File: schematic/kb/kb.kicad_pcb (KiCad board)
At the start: 2 copper layers, 13.5 x 9.8 mm, 3 parts, among them P1 USB_A, SW1 Switch_SPDT_x2

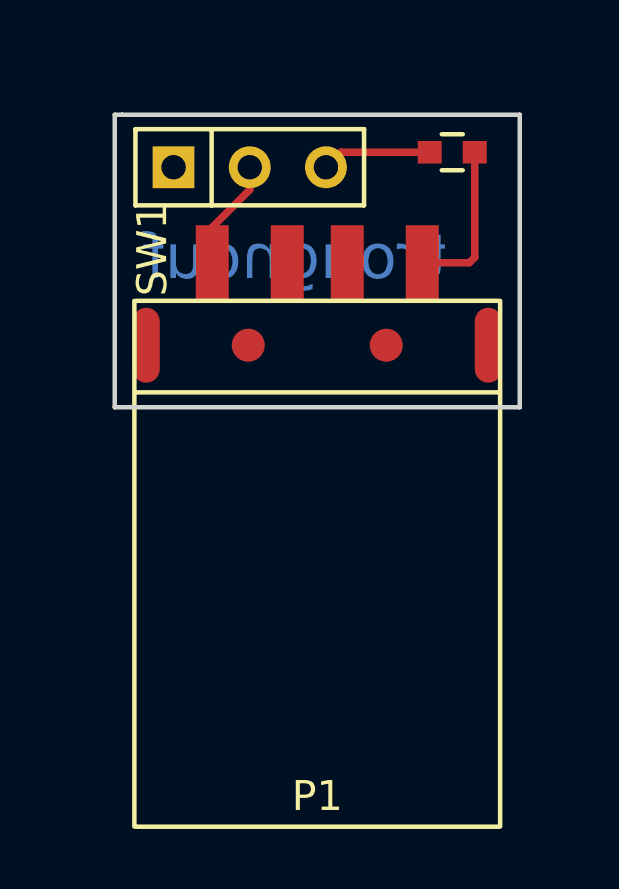
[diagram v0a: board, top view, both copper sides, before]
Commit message: Replaced single use fuse with resettable fuse (PPTC) on the keyboard-side adapter
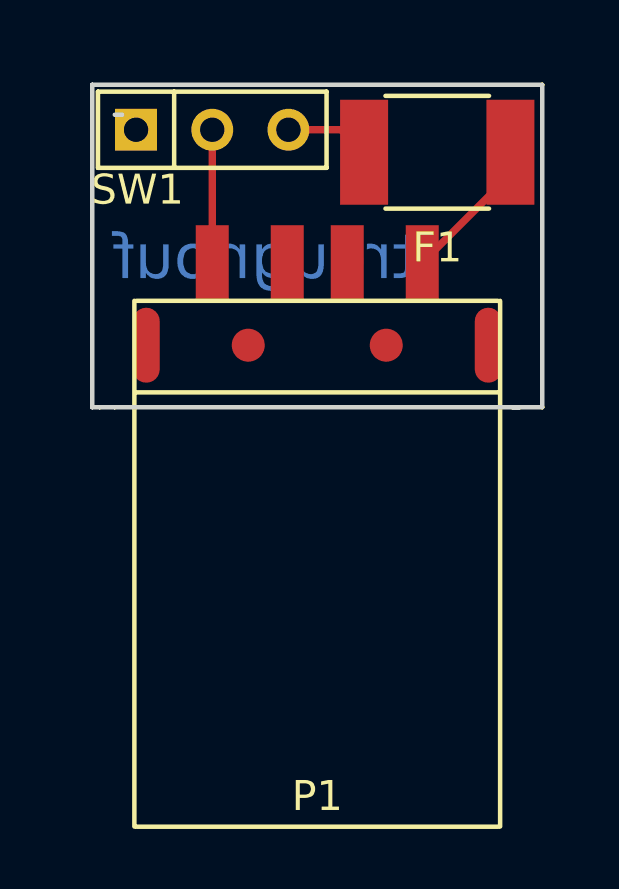
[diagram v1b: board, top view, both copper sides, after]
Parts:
- F1: value 1A -> PPTC; footprint Capacitors_SMD:C_0603 -> Resistors_SMD:R_1812
- moved SW1 1.77 mm to (145.2, 105.8)
- moved F1 0.50 mm to (152.8, 106.5)
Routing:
- net Net-(P1-Pad4): track 3.70 -> 5.61 mm
- net Net-(F1-Pad2): track 3.67 -> 2.83 mm
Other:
- board size 13.5 x 9.8 mm -> 15 x 10.8 mm
- board text added: "Use with USB-SW"
- board text removed: "To avoid autodestruction, use only with USB-SW"
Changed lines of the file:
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@@
     (links 4)
     (no_connects 1)
-    (area 0 0 0 0)
+    (area 141.924999 105.174999 155.575001 115.075001)
     (thickness 1.6)
-    (drawings 7)
-    (tracks 8)
+    (drawings 13)
+    (tracks 6)
     (zones 0)
     (modules 3)
@@
   )
   (module Buttons_Switches_ThroughHole:SW_Micro_SPST (layer F.Cu)
-    (at 146.5 107)
+    (at 145.25 105.75)
     (tags "Switch Micro SPST")
-    (fp_text reference SW1 (at -3.25 2.75 90) (layer F.SilkS)
+    (fp_text reference SW1 (at -2.5 2 180) (layer F.SilkS)
       (effects (font (size 1 1) (thickness 0.15)))
     )
@@
     )
   )
-  (module Capacitors_SMD:C_0603 (layer F.Cu)
-    (at 153.25 106.5 180)
-    (descr "Capacitor SMD 0603, reflow soldering, AVX (see smccp.pdf)")
-    (tags "capacitor 0603")
-    (attr smd)
-    (fp_text reference F1 (at -2.75 -3 180) (layer F.SilkS) hide
-      (effects (font (size 1 1) (thickness 0.15)))
-    )
-    (fp_text value 1A (at 2 0 270) (layer F.Fab)
-      (effects (font (size 1 1) (thickness 0.15)))
-    )
-    (fp_line (start -1.45 -0.75) (end 1.45 -0.75) (layer F.CrtYd) (width 0.05))
-    (fp_line (start -1.45 0.75) (end 1.45 0.75) (layer F.CrtYd) (width 0.05))
-    (fp_line (start -1.45 -0.75) (end -1.45 0.75) (layer F.CrtYd) (width 0.05))
-    (fp_line (start 1.45 -0.75) (end 1.45 0.75) (layer F.CrtYd) (width 0.05))
-    (fp_line (start -0.35 -0.6) (end 0.35 -0.6) (layer F.SilkS) (width 0.15))
-    (fp_line (start 0.35 0.6) (end -0.35 0.6) (layer F.SilkS) (width 0.15))
-    (pad 1 smd rect (at -0.75 0 180) (size 0.8 0.75) (layers F.Cu F.Paste F.Mask)
-      (net 1 "Net-(F1-Pad1)"))
-    (pad 2 smd rect (at 0.75 0 180) (size 0.8 0.75) (layers F.Cu F.Paste F.Mask)
-      (net 2 "Net-(F1-Pad2)"))
-    (model Capacitors_SMD.3dshapes/C_0603.wrl
-      (at (xyz 0 0 0))
-      (scale (xyz 1 1 1))
-      (rotate (xyz 0 0 0))
-    )
-  )
   (module con-trougnouf:USB_A (layer F.Cu)
     (at 148.75 114.5)
@@
       (effects (font (size 1 1) (thickness 0.15)))
     )
-    (fp_text value USB_A (at 5.25 -5 90) (layer F.Fab)
+    (fp_text value USB_A (at -5.25 -3.75 180) (layer F.Fab)
       (effects (font (size 1 1) (thickness 0.15)))
     )
@@
       (net 3 "Net-(P1-Pad5)"))
   )
-  (gr_line (start 142 105.25) (end 142 115) (angle 90) (layer Edge.Cuts) (width 0.15))
+  (module Resistors_SMD:R_1812 (layer F.Cu)
+    (at 152.75 106.5 180)
+    (descr "Resistor SMD 1812, flow soldering, Panasonic (see ERJ12)")
+    (tags "resistor 1812")
+    (attr smd)
+    (fp_text reference F1 (at 0 -3.175 180) (layer F.SilkS)
+      (effects (font (size 1 1) (thickness 0.15)))
+    )
+    (fp_text value PPTC (at -1.5 -3 180) (layer F.Fab)
+      (effects (font (size 1 1) (thickness 0.15)))
+    )
+    (fp_line (start -3.5052 -2.2352) (end 3.5052 -2.2352) (layer F.CrtYd) (width 0.05))
+    (fp_line (start 3.5052 -2.2352) (end 3.5052 2.2352) (layer F.CrtYd) (width 0.05))
+    (fp_line (start 3.5052 2.2352) (end -3.5052 2.2352) (layer F.CrtYd) (width 0.05))
+    (fp_line (start -3.5052 2.2352) (end -3.5052 -2.2352) (layer F.CrtYd) (width 0.05))
+    (fp_line (start -1.7272 1.8796) (end 1.7272 1.8796) (layer F.SilkS) (width 0.15))
+    (fp_line (start -1.7272 -1.8796) (end 1.7272 -1.8796) (layer F.SilkS) (width 0.15))
+    (pad 1 smd rect (at -2.4384 0 180) (size 1.6 3.5) (layers F.Cu F.Paste F.Mask)
+      (net 1 "Net-(F1-Pad1)"))
+    (pad 2 smd rect (at 2.4384 0 180) (size 1.6 3.5) (layers F.Cu F.Paste F.Mask)
+      (net 2 "Net-(F1-Pad2)"))
+  )
+  (gr_arc (start 154.25 105.5) (end 155.75 109) (angle 120) (layer B.Mask) (width 0.2))
+  (gr_circle (center 152.75 105.5) (end 153 106.25) (layer B.Mask) (width 0.2))
+  (gr_circle (center 154.75 106.25) (end 155.25 106.5) (layer B.Mask) (width 0.2))
+  (gr_line (start 156.25 115) (end 155.25 115) (angle 90) (layer Edge.Cuts) (width 0.15))
+  (gr_line (start 156.25 104.25) (end 156.25 115) (angle 90) (layer Edge.Cuts) (width 0.15))
+  (gr_line (start 141.25 104.25) (end 156.25 104.25) (angle 90) (layer Edge.Cuts) (width 0.15))
+  (gr_line (start 141.25 115) (end 141.25 104.25) (angle 90) (layer Edge.Cuts) (width 0.15))
+  (gr_line (start 141.5 115) (end 141.25 115) (angle 90) (layer Edge.Cuts) (width 0.15))
+  (gr_line (start 142 115) (end 141.5 115) (angle 90) (layer Edge.Cuts) (width 0.15))
   (gr_line (start 142.25 105.25) (end 142 105.25) (angle 90) (layer Edge.Cuts) (width 0.15))
-  (gr_line (start 155.5 105.25) (end 142.25 105.25) (angle 90) (layer Edge.Cuts) (width 0.15))
-  (gr_line (start 155.5 115) (end 155.5 105.25) (angle 90) (layer Edge.Cuts) (width 0.15))
   (gr_line (start 155.5 115) (end 142 115) (angle 90) (layer Edge.Cuts) (width 0.15))
-  (gr_text "To avoid autodestruction,\nuse only with USB-SW" (at 148.25 108.5) (layer B.SilkS)
+  (gr_text "Use with USB-SW" (at 145.25 108) (layer B.SilkS)
     (effects (font (size 0.5 0.5) (thickness 0.125)) (justify mirror))
   )
-  (gr_text trougnouf (at 148 110) (layer B.Cu)
+  (gr_text trougnouf (at 147 110) (layer B.Cu)
     (effects (font (size 1.5 1.5) (thickness 0.3)) (justify mirror))
   )
-  (segment (start 152.25 110.182) (end 153.818 110.182) (width 0.25) (layer F.Cu) (net 1) (status 400000))
-  (segment (start 154 110) (end 154 106.5) (width 0.25) (layer F.Cu) (net 1) (status 800000))
-  (segment (start 153.818 110.182) (end 154 110) (width 0.25) (layer F.Cu) (net 1))
-  (segment (start 152.5 106.5) (end 149.54 106.5) (width 0.25) (layer F.Cu) (net 2) (status 400000))
-  (segment (start 149.54 106.5) (end 149.04 107) (width 0.25) (layer F.Cu) (net 2) (status 800000))
-  (segment (start 146.5 107) (end 146.5 107.75) (width 0.25) (layer F.Cu) (net 4) (status 400000))
-  (segment (start 146.5 107.75) (end 145.25 109) (width 0.25) (layer F.Cu) (net 4) (status 800000))
-  (segment (start 145.25 109) (end 145.25 110.182) (width 0.25) (layer F.Cu) (net 4) (status C00000))
+  (segment (start 155.1884 106.5) (end 155.1884 107.2436) (width 0.25) (layer F.Cu) (net 1) (status C00000))
+  (segment (start 155.1884 107.2436) (end 152.25 110.182) (width 0.25) (layer F.Cu) (net 1) (status C00000))
+  (segment (start 147.79 105.75) (end 149.5616 105.75) (width 0.25) (layer F.Cu) (net 2) (status C00000))
+  (segment (start 149.5616 105.75) (end 150.3116 106.5) (width 0.25) (layer F.Cu) (net 2) (status C00000))
+  (segment (start 145.25 105.75) (end 145.25 110.182) (width 0.25) (layer F.Cu) (net 4) (status C00000))
+  (segment (start 145.25 109) (end 145.25 110.182) (width 0.25) (layer F.Cu) (net 4))
 )

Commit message: Added a red LED and matching resistor to warn user when USB splitter is missing
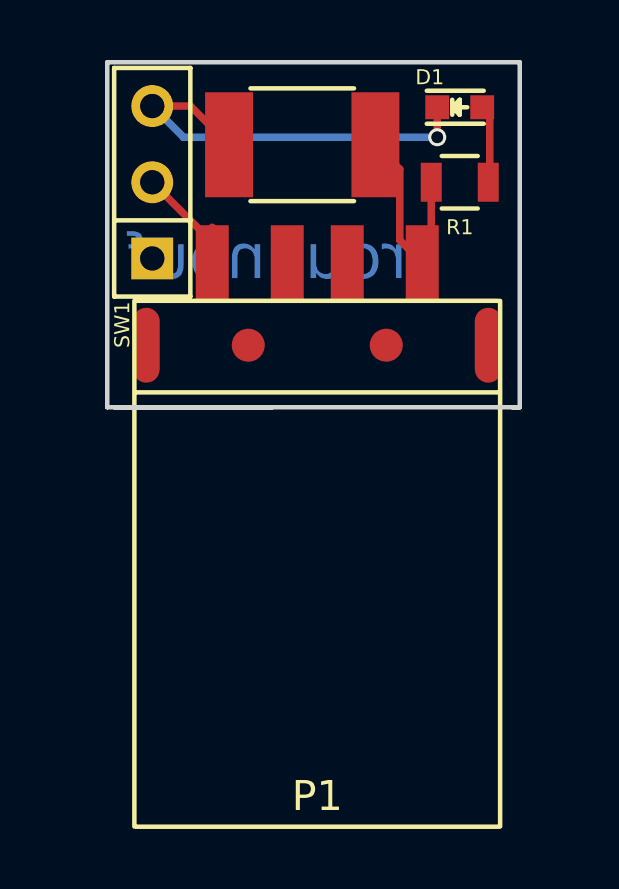
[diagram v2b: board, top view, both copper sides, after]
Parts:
- removed F1: PPTC, Resistors_SMD:R_1812
- added D1: LED, LEDs:LED-0603, F.Cu at (153.5, 105.0)
- added R1: 150, Resistors_SMD:R_0805, F.Cu at (153.5, 107.5)
- added R2: PPTC, Resistors_SMD:R_1812, F.Cu at (148.2, 106.2)
- moved SW1 2.66 mm to (143.2, 107.5), turned to 90 degrees
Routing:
- net Net-(D1-Pad1): track 2.83 -> 14.0 mm, vias 0 -> 1
- net Net-(D1-Pad2): track 0.00 -> 2.91 mm
- net Net-(P1-Pad1): track 4.90 -> 7.39 mm
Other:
- board size 15 x 10.8 mm -> 13.8 x 11.5 mm

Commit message: Better fit for the text
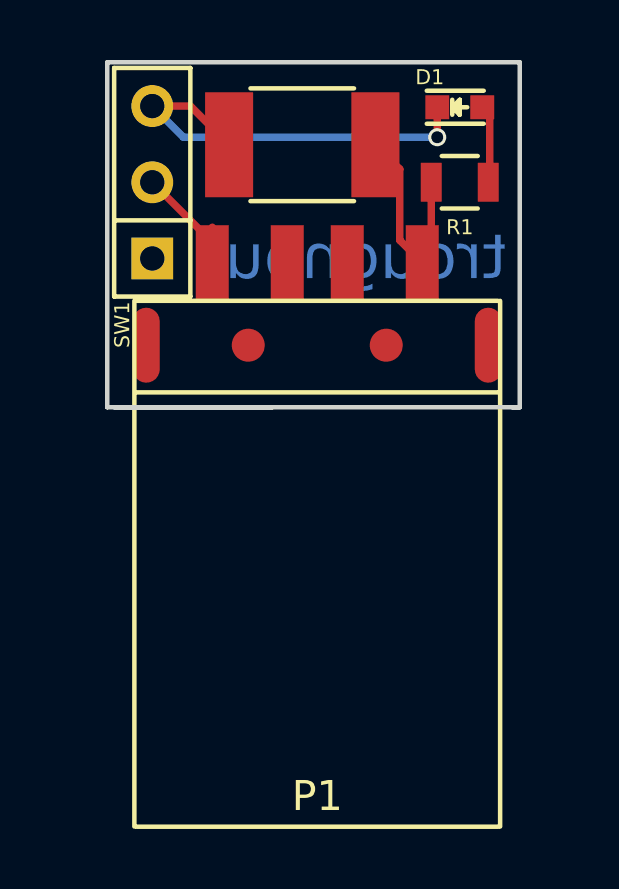
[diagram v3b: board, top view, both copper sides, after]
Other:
- board text added: "USB-SW(KB) 1.00"
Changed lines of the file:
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@@
     (links 7)
     (no_connects 1)
-    (area 141.174999 114.924999 156.325001 115.075001)
+    (area 141.5125 101.295237 155.850001 129.257001)
     (thickness 1.6)
-    (drawings 13)
+    (drawings 14)
     (tracks 22)
     (zones 0)
@@
       (net 8 "Net-(P1-Pad1)"))
   )
+  (gr_text "USB-SW(KB) 1.00" (at 148.25 104) (layer B.SilkS)
+    (effects (font (size 0.5 0.5) (thickness 0.125)) (justify mirror))
+  )
   (gr_line (start 155.25 115) (end 155.5 115) (angle 90) (layer Edge.Cuts) (width 0.15))
   (gr_line (start 144.25 115) (end 147.25 115) (angle 90) (layer Edge.Cuts) (width 0.15))
@@
     (effects (font (size 0.5 0.5) (thickness 0.125)) (justify mirror))
   )
-  (gr_text trougnouf (at 147.5 110) (layer B.Cu)
+  (gr_text trougnouf (at 150 110) (layer B.Cu)
     (effects (font (size 1.5 1.5) (thickness 0.3)) (justify mirror))
   )
